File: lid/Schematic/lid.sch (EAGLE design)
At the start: 13 parts, among them Q1 IRL540

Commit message: Update lid.sch
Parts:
- added JP1: (no value), adafruit:PINHD-1X1
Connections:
- net N$9: now also JP1.1
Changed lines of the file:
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@@
 <part name="JP4" library="pinhead" library_urn="urn:adsk.eagle:library:325" deviceset="PINHD-1X4" device="" package3d_urn="urn:adsk.eagle:package:22407/2"/>
 <part name="X_3" library="ngspice-simulation" library_urn="urn:adsk.eagle:library:527439" deviceset="GND" device=""/>
+<part name="JP1" library="adafruit" deviceset="PINHD-1X1" device=""/>
 </parts>
 <sheets>
@@
 <text x="22.606" y="105.918" size="1.778" layer="95">D6</text>
 <text x="22.606" y="103.378" size="1.778" layer="95">D5</text>
-<text x="20.32" y="114.3" size="1.778" layer="97">For LED and
+<text x="10.16" y="121.92" size="1.778" layer="97">For LED and
 Fan control</text>
+<text x="19.812" y="113.03" size="1.778" layer="95">Action</text>
 </plain>
 <instances>
@@
 <instance part="ACTION" gate="G$1" x="109.22" y="76.2" smashed="yes" rot="R270"/>
 <instance part="JP4" gate="A" x="27.94" y="106.68" smashed="yes" rot="R180">
-<attribute name="NAME" x="34.29" y="98.425" size="1.778" layer="95" rot="R180"/>
 <attribute name="VALUE" x="34.29" y="114.3" size="1.778" layer="96" rot="R180"/>
 </instance>
 <instance part="X_3" gate="G$1" x="38.1" y="58.42" smashed="yes"/>
+<instance part="JP1" gate="G$1" x="27.94" y="114.3" smashed="yes" rot="R180">
+<attribute name="VALUE" x="34.29" y="119.38" size="1.778" layer="96" rot="R180"/>
+</instance>
 </instances>
 <busses>
@@
 <pinref part="W1" gate="G$1" pin="D4"/>
 <wire x1="109.22" y1="99.06" x2="96.52" y2="99.06" width="0.1524" layer="91"/>
-</segment>
-</net>
+<pinref part="JP1" gate="G$1" pin="1"/>
+<wire x1="30.48" y1="114.3" x2="48.26" y2="114.3" width="0.1524" layer="91"/>
+<wire x1="48.26" y1="114.3" x2="48.26" y2="134.62" width="0.1524" layer="91"/>
+<wire x1="48.26" y1="134.62" x2="109.22" y2="134.62" width="0.1524" layer="91"/>
+<wire x1="109.22" y1="134.62" x2="109.22" y2="99.06" width="0.1524" layer="91"/>
+<junction x="109.22" y="99.06"/>
+</segment>
+</net>

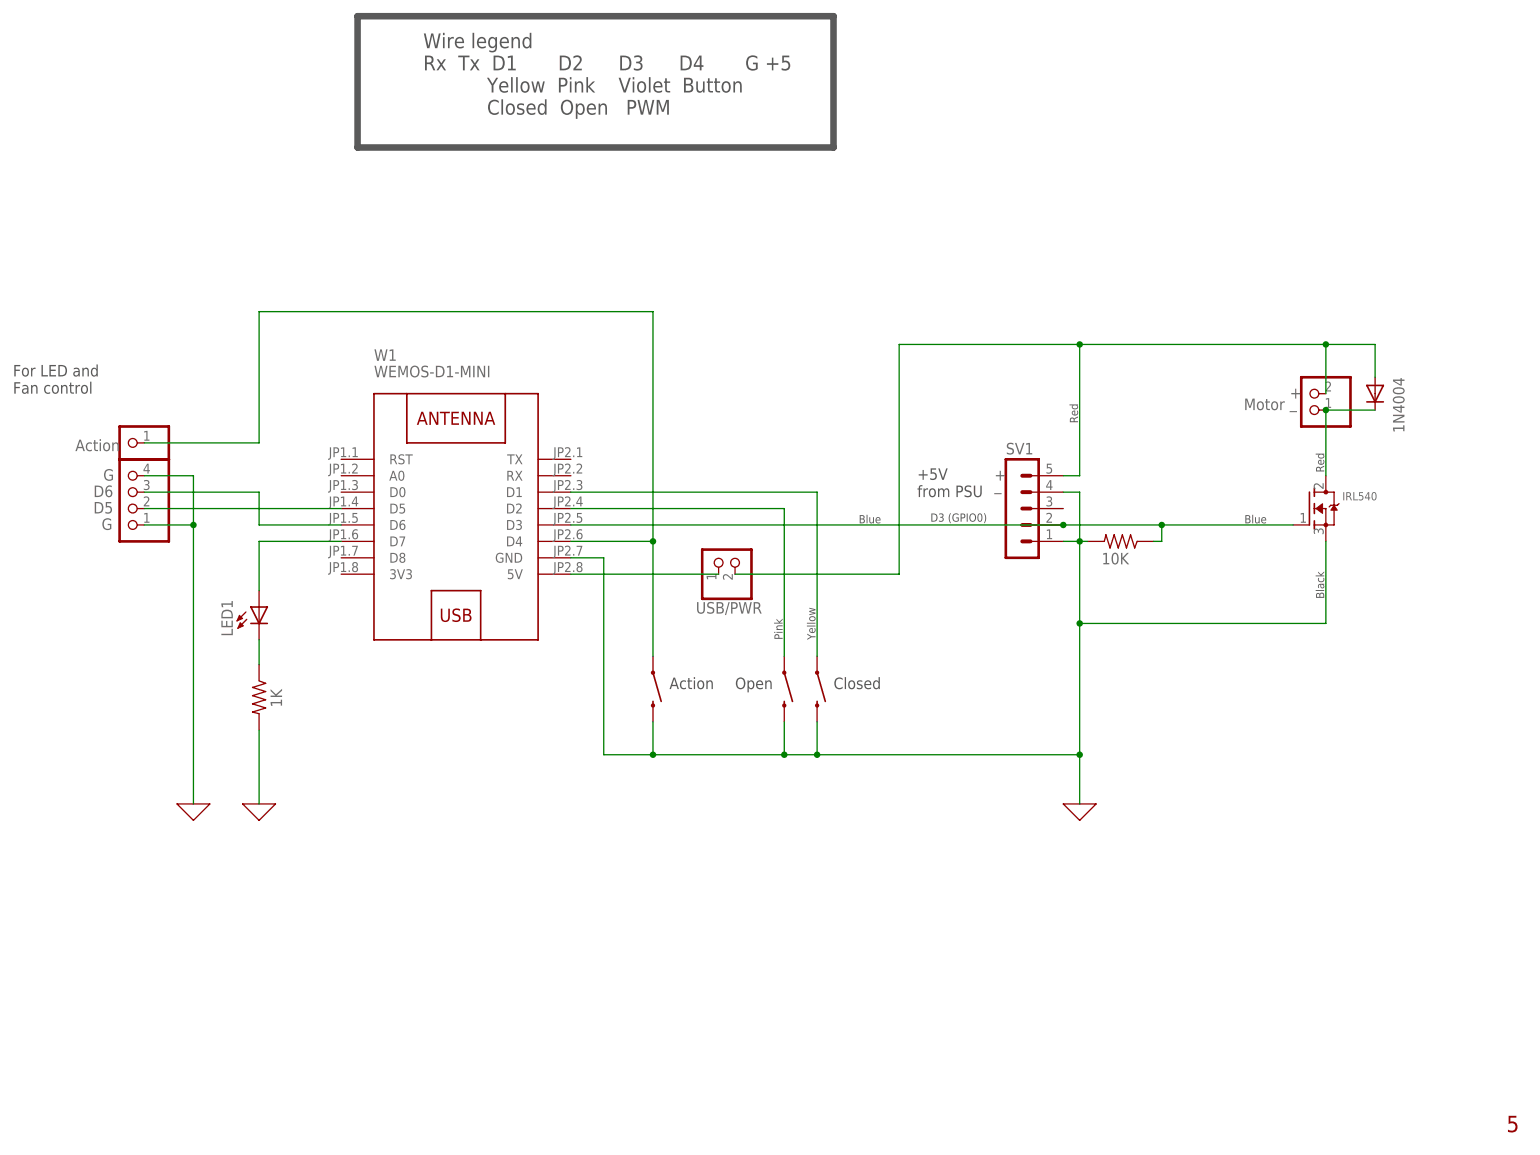
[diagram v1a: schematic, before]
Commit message: Made dfplayer2 from dfplayer, without mqtt or console menu.
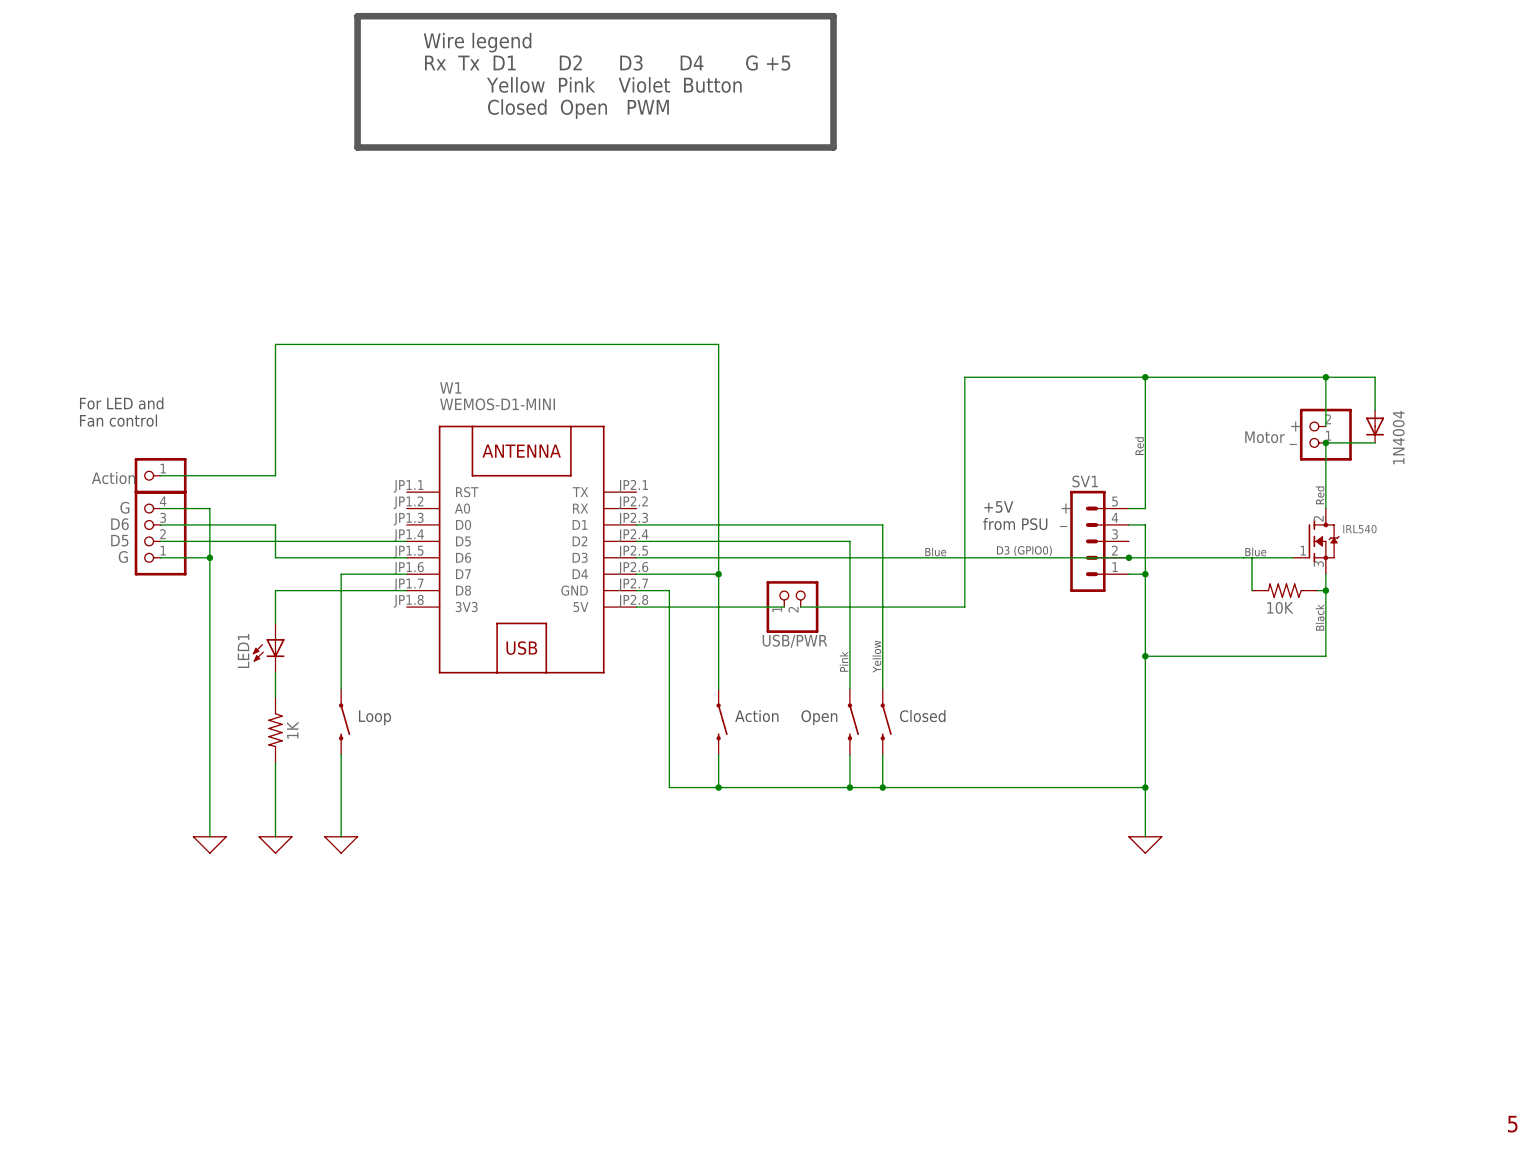
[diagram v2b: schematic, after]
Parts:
- added ACTION1: MOMENTARY-SWITCH-SPST-PTH-6.0MM, SparkFun-Switches:MOMENTARY-SWITCH-SPST-PTH-6.0MM
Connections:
- new net N$12: ACTION1.1, W1.D7
- net 0: now also ACTION1.2, R4.1; no longer R4.2
- net N$1: now also R4.2; no longer R4.1
- net N$6: now also W1.D8; no longer W1.D7
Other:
- note added: "Loop"
- moved on the sheet: LED1, SV1, USB/PWR, W1
